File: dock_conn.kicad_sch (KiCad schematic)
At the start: 1 part, among them J10 Conn_02x35_Odd_Even

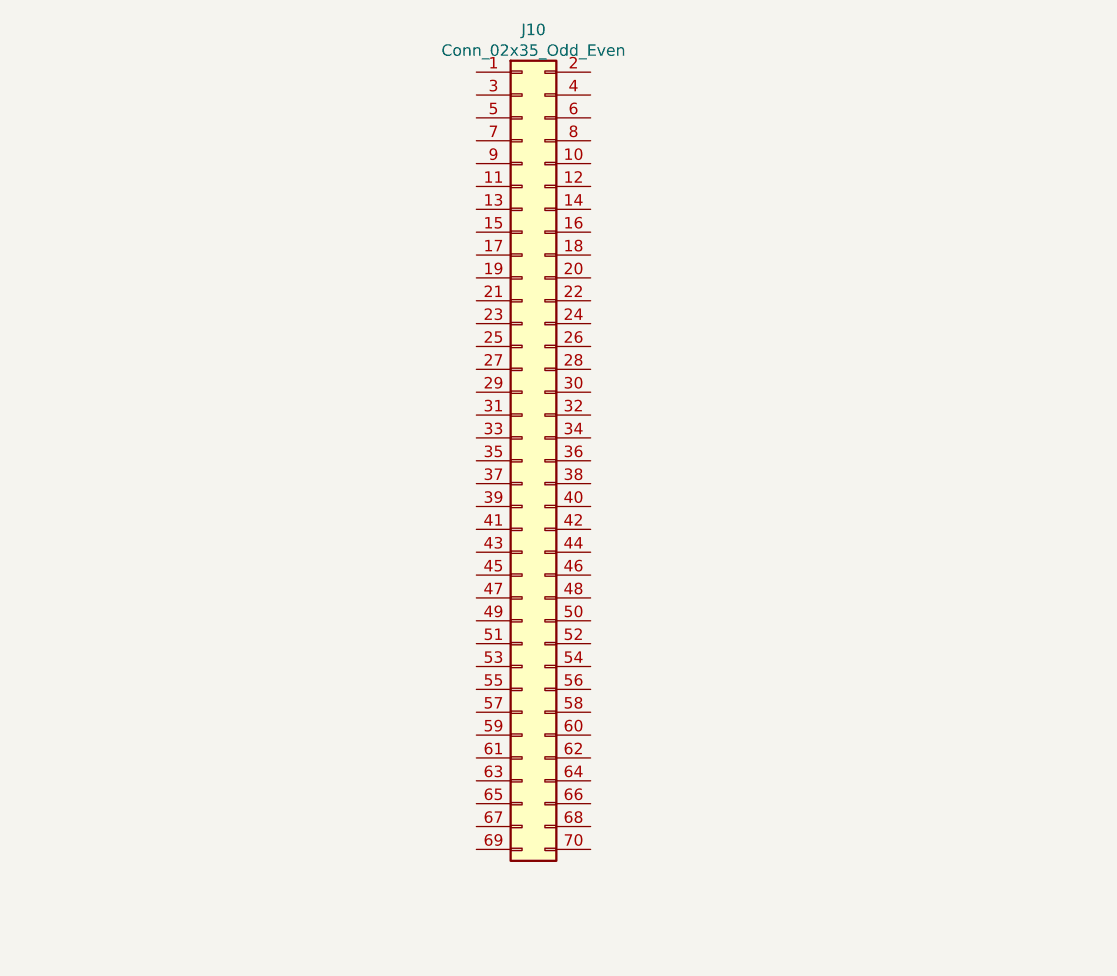
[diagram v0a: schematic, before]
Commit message: Add pinouts for dock connector; rearrange LCD backlight driver; copy the bq25895 schematic from SuperPower-RPi and add schottky to support 3.1A output on PMID.
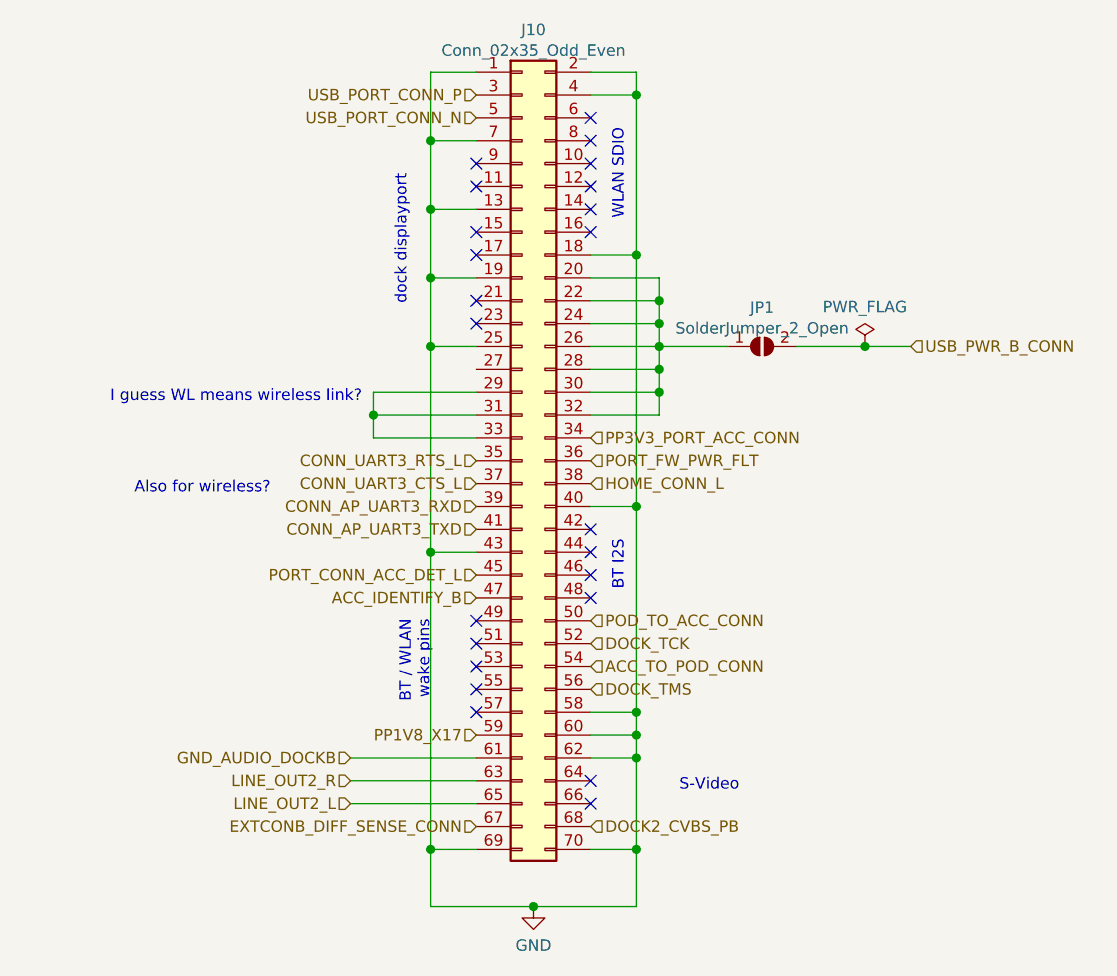
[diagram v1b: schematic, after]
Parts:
- added JP1: SolderJumper_2_Open, Jumper:SolderJumper-2_P1.3mm_Open_RoundedPad1.0x1.5mm, symbol Jumper:SolderJumper_2_Open
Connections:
- net GND: now reaches J10.1 (Pin_1)
- net GND: now also J10.13 (Pin_13), J10.18 (Pin_18), J10.19 (Pin_19), J10.2 (Pin_2), J10.25 (Pin_25), J10.4 (Pin_4), J10.40 (Pin_40), J10.43 (Pin_43), J10.58 (Pin_58), J10.60 (Pin_60), J10.62 (Pin_62), J10.69 (Pin_69), J10.7 (Pin_7), J10.70 (Pin_70)
- net at J10.20 (Pin_20): now also J10.22 (Pin_22), J10.24 (Pin_24), J10.26 (Pin_26), J10.28 (Pin_28), J10.30 (Pin_30), J10.32 (Pin_32), JP1.1 (A)
- net at J10.29 (Pin_29): now also J10.31 (Pin_31), J10.33 (Pin_33)
- net USB_PORT_CONN_P: now reaches J10.3 (Pin_3)
- net PP3V3_PORT_ACC_CONN: now reaches J10.34 (Pin_34)
- net CONN_UART3_RTS_L: now reaches J10.35 (Pin_35)
- net PORT_FW_PWR_FLT: now reaches J10.36 (Pin_36)
- net CONN_UART3_CTS_L: now reaches J10.37 (Pin_37)
- net HOME_CONN_L: now reaches J10.38 (Pin_38)
- net CONN_AP_UART3_RXD: now reaches J10.39 (Pin_39)
- net CONN_AP_UART3_TXD: now reaches J10.41 (Pin_41)
- net PORT_CONN_ACC_DET_L: now reaches J10.45 (Pin_45)
- net ACC_IDENTIFY_B: now reaches J10.47 (Pin_47)
- net USB_PORT_CONN_N: now reaches J10.5 (Pin_5)
- net POD_TO_ACC_CONN: now reaches J10.50 (Pin_50)
- net DOCK_TCK: now reaches J10.52 (Pin_52)
- net ACC_TO_POD_CONN: now reaches J10.54 (Pin_54)
- net DOCK_TMS: now reaches J10.56 (Pin_56)
- net PP1V8_X17: now reaches J10.59 (Pin_59)
- net GND_AUDIO_DOCKB: now reaches J10.61 (Pin_61)
- net LINE_OUT2_R: now reaches J10.63 (Pin_63)
- net LINE_OUT2_L: now reaches J10.65 (Pin_65)
- net EXTCONB_DIFF_SENSE_CONN: now reaches J10.67 (Pin_67)
- net DOCK2_CVBS_PB: now reaches J10.68 (Pin_68)
- new net USB_PWR_B_CONN: JP1.2 (B)
- no-connect marks 0 -> 23
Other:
- note added: "Also for wireless?"
- note added: "BT / WLAN wake pins"
- note added: "BT I2S"
- note added: "I guess WL means wireless link?"
- note added: "S-Video"
- note added: "WLAN SDIO"
- note added: "dock displayport"

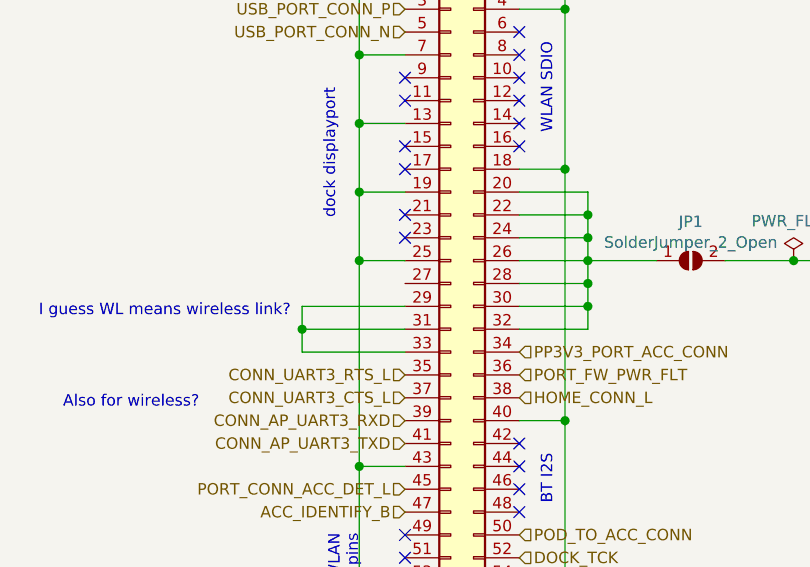
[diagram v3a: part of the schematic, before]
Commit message: Fix (or ignore) all ERC and DRC errors.
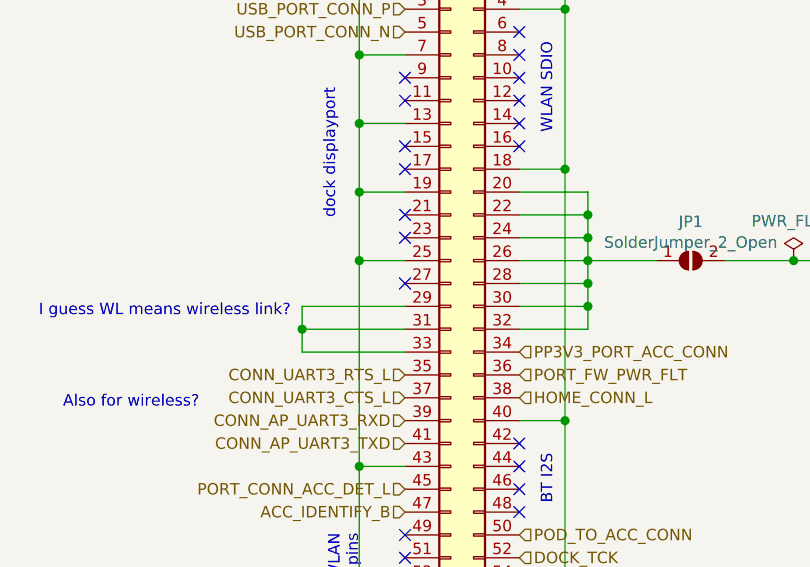
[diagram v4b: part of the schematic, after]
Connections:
- no-connect marks 23 -> 24
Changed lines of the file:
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@@
   (no_connect (at 132.08 72.39))
   (no_connect (at 132.08 74.93))
+  (no_connect (at 132.08 80.01))
   (no_connect (at 132.08 107.95))
   (no_connect (at 132.08 110.49))

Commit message: WIP: add 2230 NVMe drive footprint
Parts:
- JP1: footprint Jumper:SolderJumper-2_P1.3mm_Open_RoundedPad1.0x1.5mm -> Resistor_SMD:R_0402_1005Metric
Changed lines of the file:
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@@
     (property "Reference" "JP1" (id 0) (at 163.83 73.1478 0))
     (property "Value" "SolderJumper_2_Open" (id 1) (at 163.83 75.4465 0))
-    (property "Footprint" "Jumper:SolderJumper-2_P1.3mm_Open_RoundedPad1.0x1.5mm" (id 2) (at 163.83 77.47 0)
+    (property "Footprint" "Resistor_SMD:R_0402_1005Metric" (id 2) (at 163.83 77.47 0)
       (effects (font (size 1.27 1.27)) hide)
     )

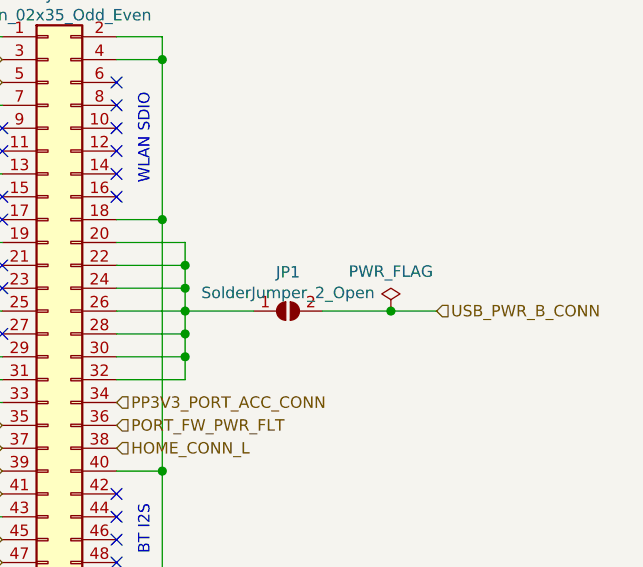
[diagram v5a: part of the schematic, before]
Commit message: Lots of changes: add USB switch in charger circuit, reroute differential pairs using proper track widths; make CM4 courtyard the full size. Fixes #11.
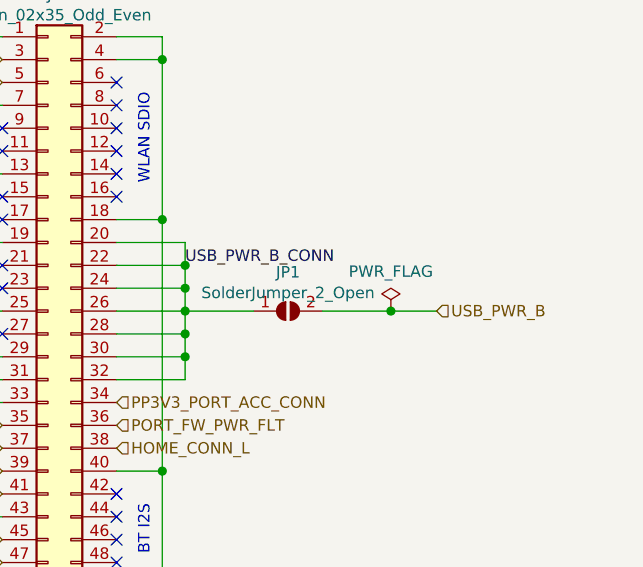
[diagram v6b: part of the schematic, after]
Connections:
- net USB_PWR_B_CONN: now also J10.20 (Pin_20), J10.22 (Pin_22), J10.24 (Pin_24), J10.26 (Pin_26), J10.28 (Pin_28), J10.30 (Pin_30), J10.32 (Pin_32), JP1.1 (A); no longer JP1.2 (B)
- new net USB_PWR_B: JP1.2 (B)
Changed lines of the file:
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@@
     (effects (font (size 1.27 1.27)) (justify right bottom))
+  )
+  (label "USB_PWR_B_CONN" (at 152.4 72.39 0)
+    (effects (font (size 1.27 1.27)) (justify left bottom))
   )
   (hierarchical_label "GND_AUDIO_DOCKB" (shape input) (at 118.11 123.19 180)
@@
     (effects (font (size 1.27 1.27)) (justify left))
   )
-  (hierarchical_label "USB_PWR_B_CONN" (shape input) (at 180.34 77.47 0)
+  (hierarchical_label "USB_PWR_B" (shape input) (at 180.34 77.47 0)
     (effects (font (size 1.27 1.27)) (justify left))
   )

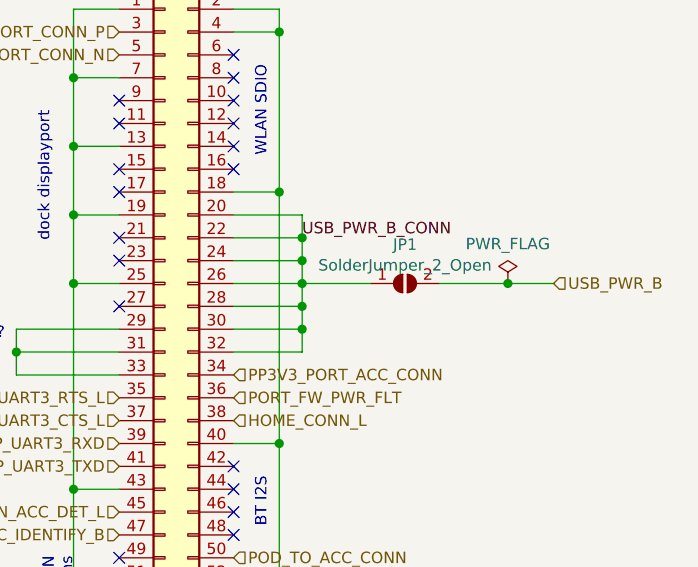
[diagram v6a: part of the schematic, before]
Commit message: Route CM4 board with differential connector on the right.
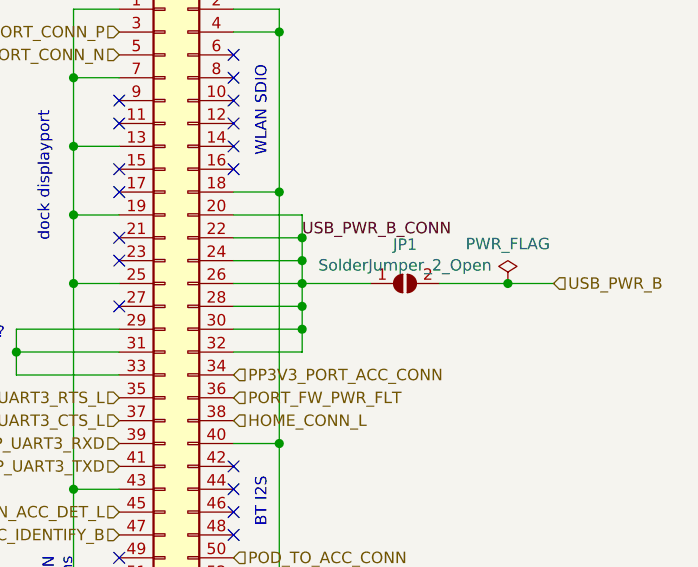
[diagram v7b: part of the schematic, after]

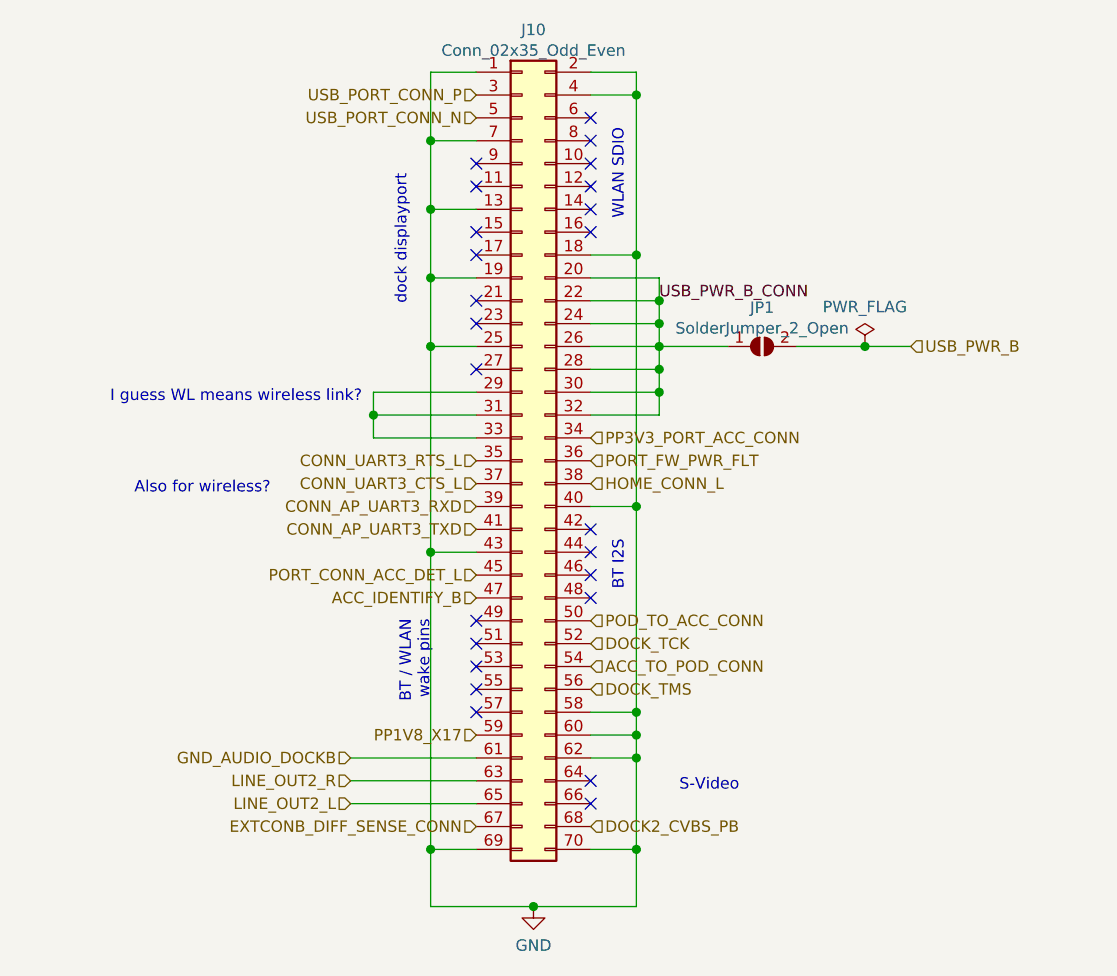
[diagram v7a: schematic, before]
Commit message: Even more testpoints!
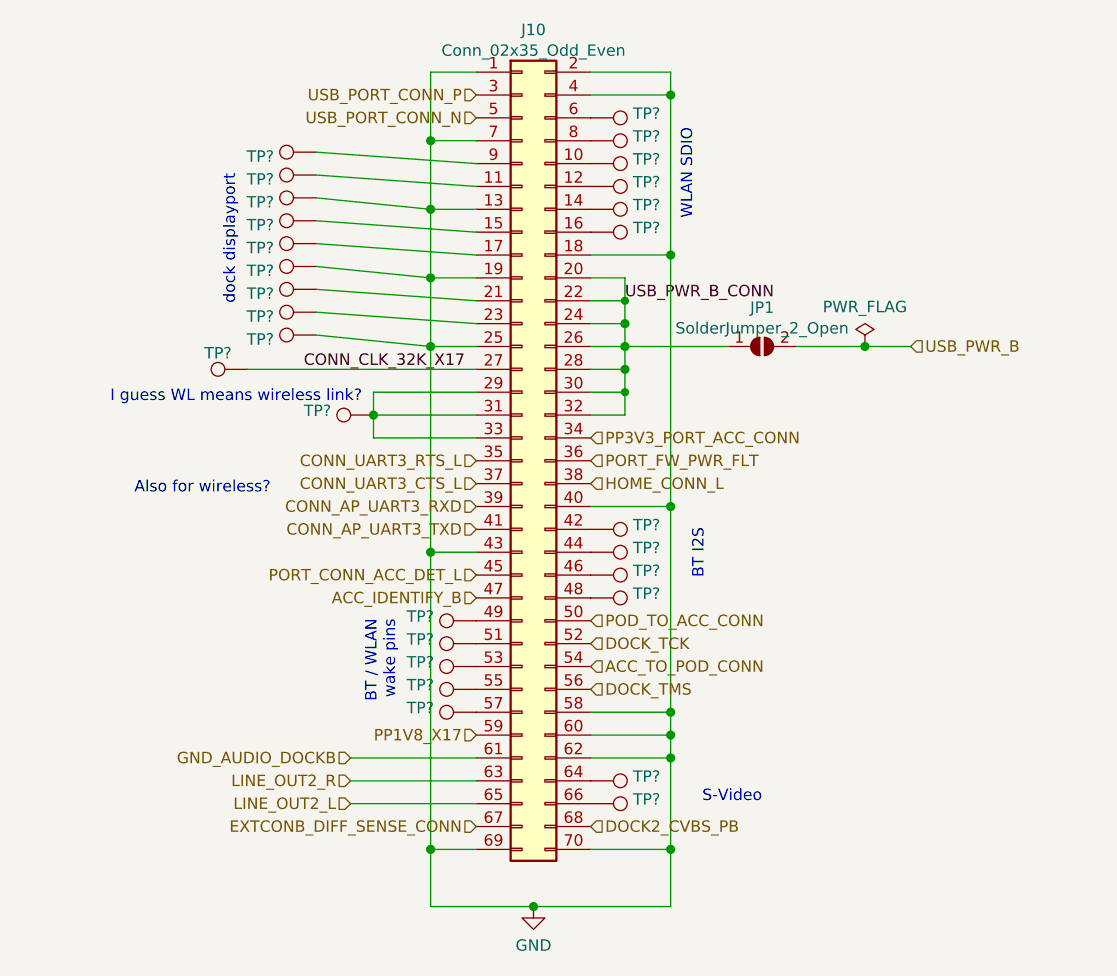
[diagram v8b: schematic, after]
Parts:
- added TP? (x28): TestPoint, footprints:testpoint_small, symbol Connector:TestPoint
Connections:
- net GND: now also TP?.1, TP?.1, TP?.1
- net at J10.10 (Pin_10): now also TP?.1
- net at J10.11 (Pin_11): now also TP?.1
- net at J10.12 (Pin_12): now also TP?.1
- net at J10.14 (Pin_14): now also TP?.1
- net at J10.15 (Pin_15): now also TP?.1
- net at J10.16 (Pin_16): now also TP?.1
- net at J10.17 (Pin_17): now also TP?.1
- net at J10.21 (Pin_21): now also TP?.1
- net at J10.23 (Pin_23): now also TP?.1
- net CONN_CLK_32K_X17: now reaches J10.27 (Pin_27)
- net CONN_CLK_32K_X17: now also TP?.1
- net at J10.29 (Pin_29), J10.31 (Pin_31), J10.33 (Pin_33): now also TP?.1
- net at J10.42 (Pin_42): now also TP?.1
- net at J10.44 (Pin_44): now also TP?.1
- net at J10.46 (Pin_46): now also TP?.1
- net at J10.48 (Pin_48): now also TP?.1
- net at J10.49 (Pin_49): now also TP?.1
- net at J10.51 (Pin_51): now also TP?.1
- net at J10.53 (Pin_53): now also TP?.1
- net at J10.55 (Pin_55): now also TP?.1
- net at J10.57 (Pin_57): now also TP?.1
- net at J10.6 (Pin_6): now also TP?.1
- net at J10.64 (Pin_64): now also TP?.1
- net at J10.66 (Pin_66): now also TP?.1
- net at J10.8 (Pin_8): now also TP?.1
- net at J10.9 (Pin_9): now also TP?.1
- no-connect marks 24 -> 0
